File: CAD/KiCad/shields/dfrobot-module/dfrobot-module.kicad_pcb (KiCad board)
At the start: 2 copper layers, 29 x 32 mm, 14 parts, among them J1 JST_XH_S3B-XH-A_1x03_P2.50mm_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, J2J3 PinHeader_1x06_P2.54mm_Vertic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, J4 PinHeader_1x02_P2.54mm_Vertic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, U1 DIP-8_W7.62mm

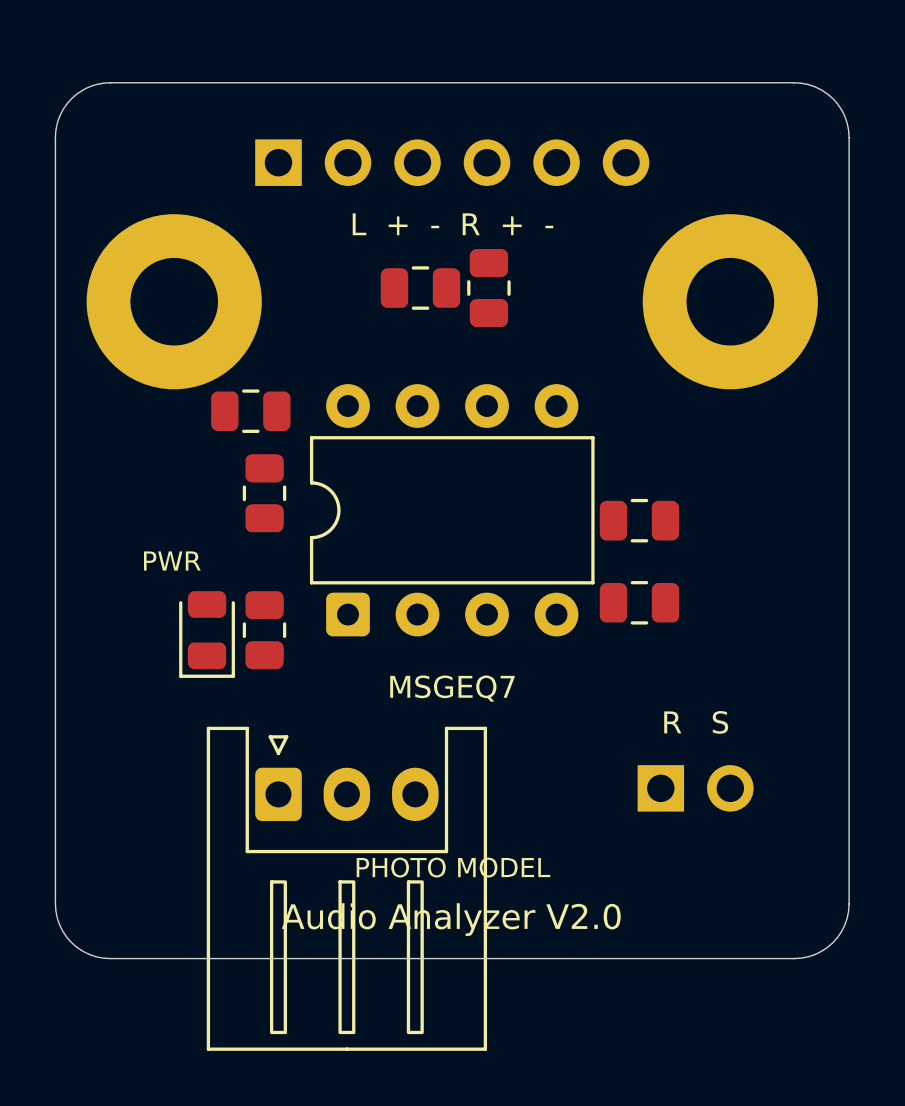
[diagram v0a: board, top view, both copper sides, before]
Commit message: Correct DFRobot reference dimensions and connectors from board comments
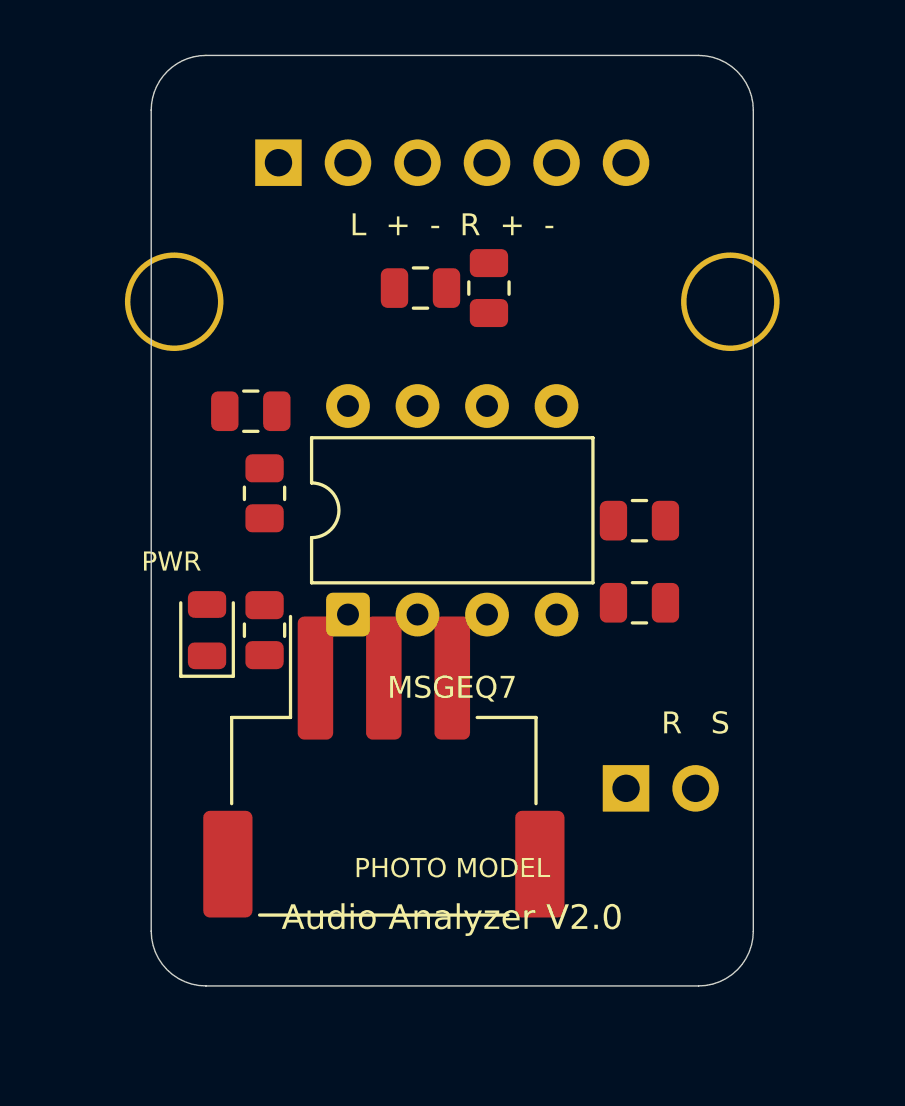
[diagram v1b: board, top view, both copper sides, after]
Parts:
- J1: value JST_XH_S3B-XH-A_1x03_P2.50mm_Horizontal -> JST_XH_S3B-XH-SM4-TB_1x03-1MP_P2.50mm_Horizontal; footprint JST_XH_S3B-XH-A_1x03_P2.50mm_Horizontal -> JST_XH_S3B-XH-SM4-TB_1x03-1MP_P2.50mm_Horizontal
- moved J1 3.98 mm to (62.0, 75.0)
- moved J4 1.27 mm to (70.8, 75.8)
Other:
- board size 29 x 32 mm -> 22 x 34 mm
- board text added: "The J2J3 pin 6 should be aligned. with the J4 pin 1 along the y axis here. I moved the J4 check that."
- board text added: "The width is 22mm not 27 The length is 34 not 32 The J1 is SMD and doesn't go outside the board."
